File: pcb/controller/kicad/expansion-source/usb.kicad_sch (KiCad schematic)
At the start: 13 parts, among them J4 USB4105-GF-A, U7 SN74LVC1G14DBVR, U8 FSUSB42MUX, U9 USBLC6-2SC6

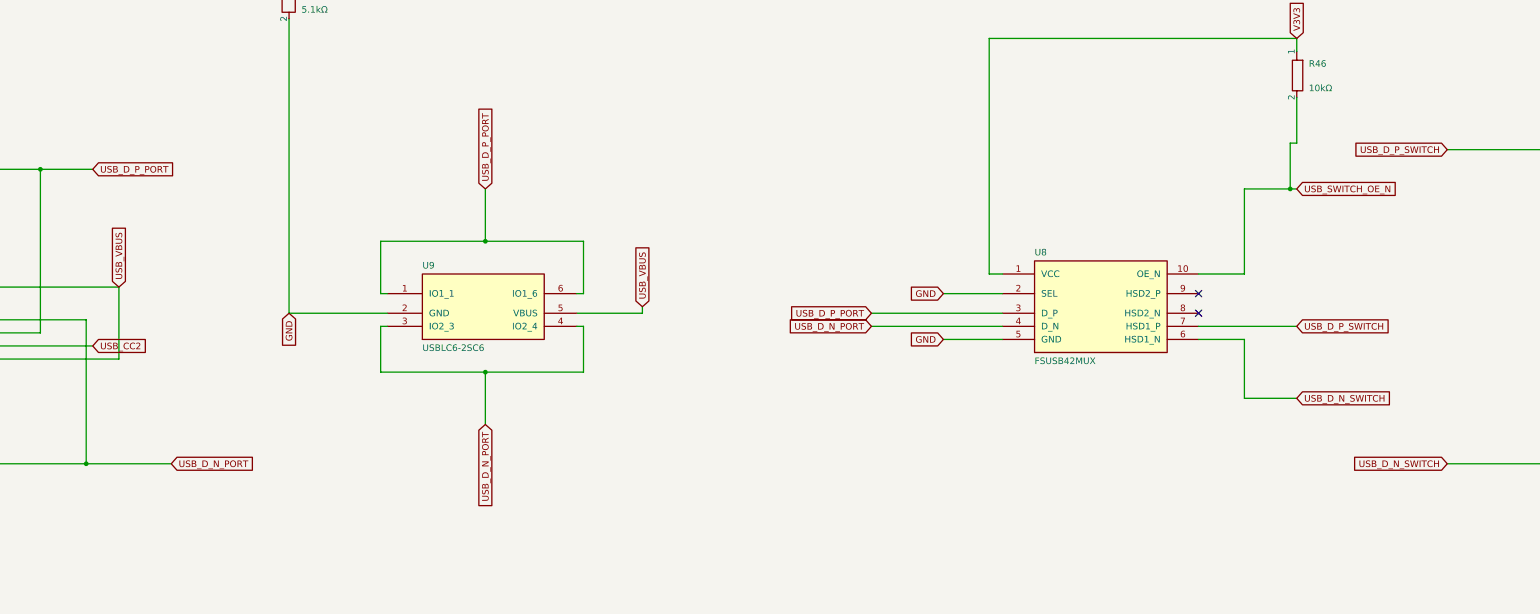
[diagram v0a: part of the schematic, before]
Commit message: Prepare filled planes and enforce KiCad routing guardrails
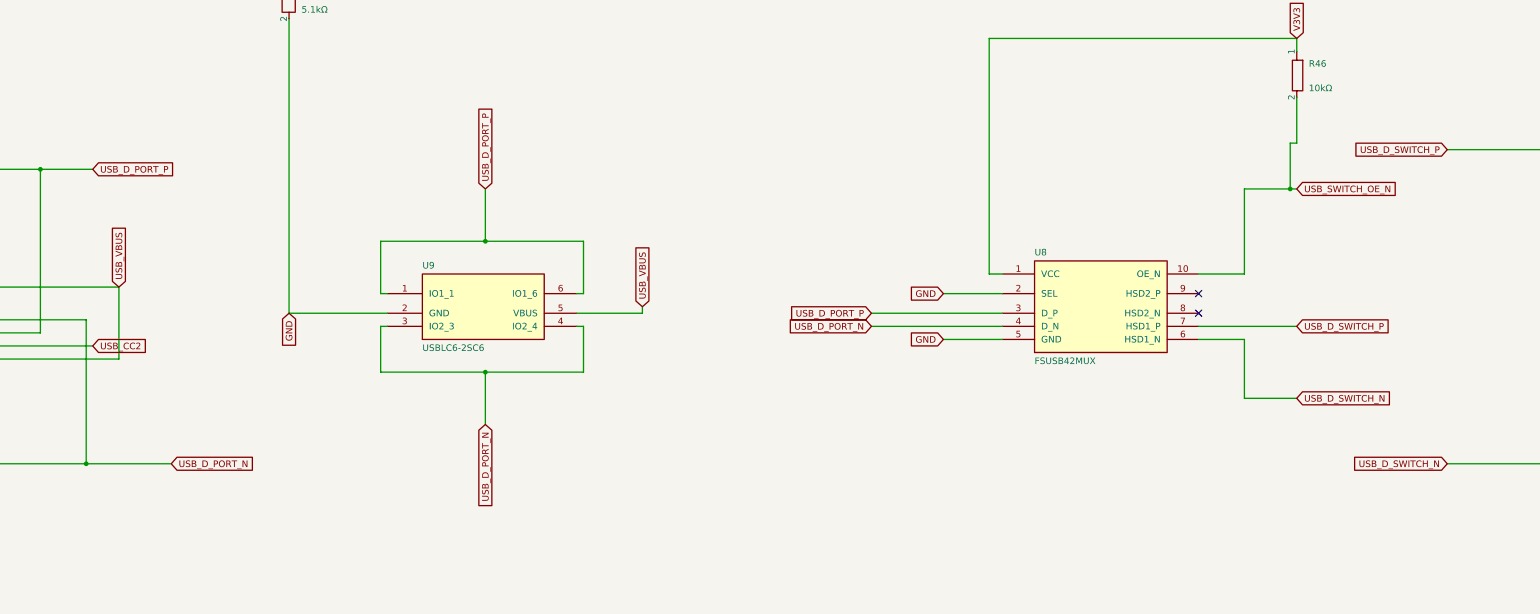
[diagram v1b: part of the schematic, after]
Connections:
- net USB_D_N_PORT renamed USB_D_PORT_N
- net USB_D_N_SWITCH renamed USB_D_SWITCH_N
- net USB_D_P_PORT renamed USB_D_PORT_P
- net USB_D_P_SWITCH renamed USB_D_SWITCH_P
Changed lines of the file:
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@@
 		)
 	)
-	(global_label "USB_D_P_SWITCH"
+	(global_label "USB_D_SWITCH_P"
 		(shape input)
 		(at 431.8 128.27 180)
@@
 		)
 	)
-	(global_label "USB_D_P_SWITCH"
+	(global_label "USB_D_SWITCH_P"
 		(shape input)
 		(at 402.59 162.56 0)
@@
 		)
 	)
-	(global_label "USB_D_P_PORT"
+	(global_label "USB_D_PORT_P"
 		(shape input)
 		(at 245.11 135.89 90)
@@
 		)
 	)
-	(global_label "USB_D_P_PORT"
+	(global_label "USB_D_PORT_P"
 		(shape input)
 		(at 320.04 160.02 180)
@@
 		)
 	)
-	(global_label "USB_D_N_PORT"
+	(global_label "USB_D_PORT_N"
 		(shape input)
 		(at 245.11 181.61 270)
@@
 		)
 	)
-	(global_label "USB_D_P_PORT"
+	(global_label "USB_D_PORT_P"
 		(shape input)
 		(at 168.91 132.08 0)
@@
 		)
 	)
-	(global_label "USB_D_N_SWITCH"
+	(global_label "USB_D_SWITCH_N"
 		(shape input)
 		(at 431.8 189.23 180)
@@
 		)
 	)
-	(global_label "USB_D_N_PORT"
+	(global_label "USB_D_PORT_N"
 		(shape input)
 		(at 184.15 189.23 0)
@@
 		)
 	)
-	(global_label "USB_D_N_PORT"
+	(global_label "USB_D_PORT_N"
 		(shape input)
 		(at 320.04 162.56 180)
@@
 		)
 	)
-	(global_label "USB_D_N_SWITCH"
+	(global_label "USB_D_SWITCH_N"
 		(shape input)
 		(at 402.59 176.53 0)
